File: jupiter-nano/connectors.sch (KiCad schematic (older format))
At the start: 21 parts, among them J1 USB_B_Micro, J2 USB_B_Micro, J3 Conn_ARM_JTAG_SWD_10, J4 USB_B_Micro, J5 Micro_SD_Card_Det_Hirose_DM3AT, J6 Conn_01x02

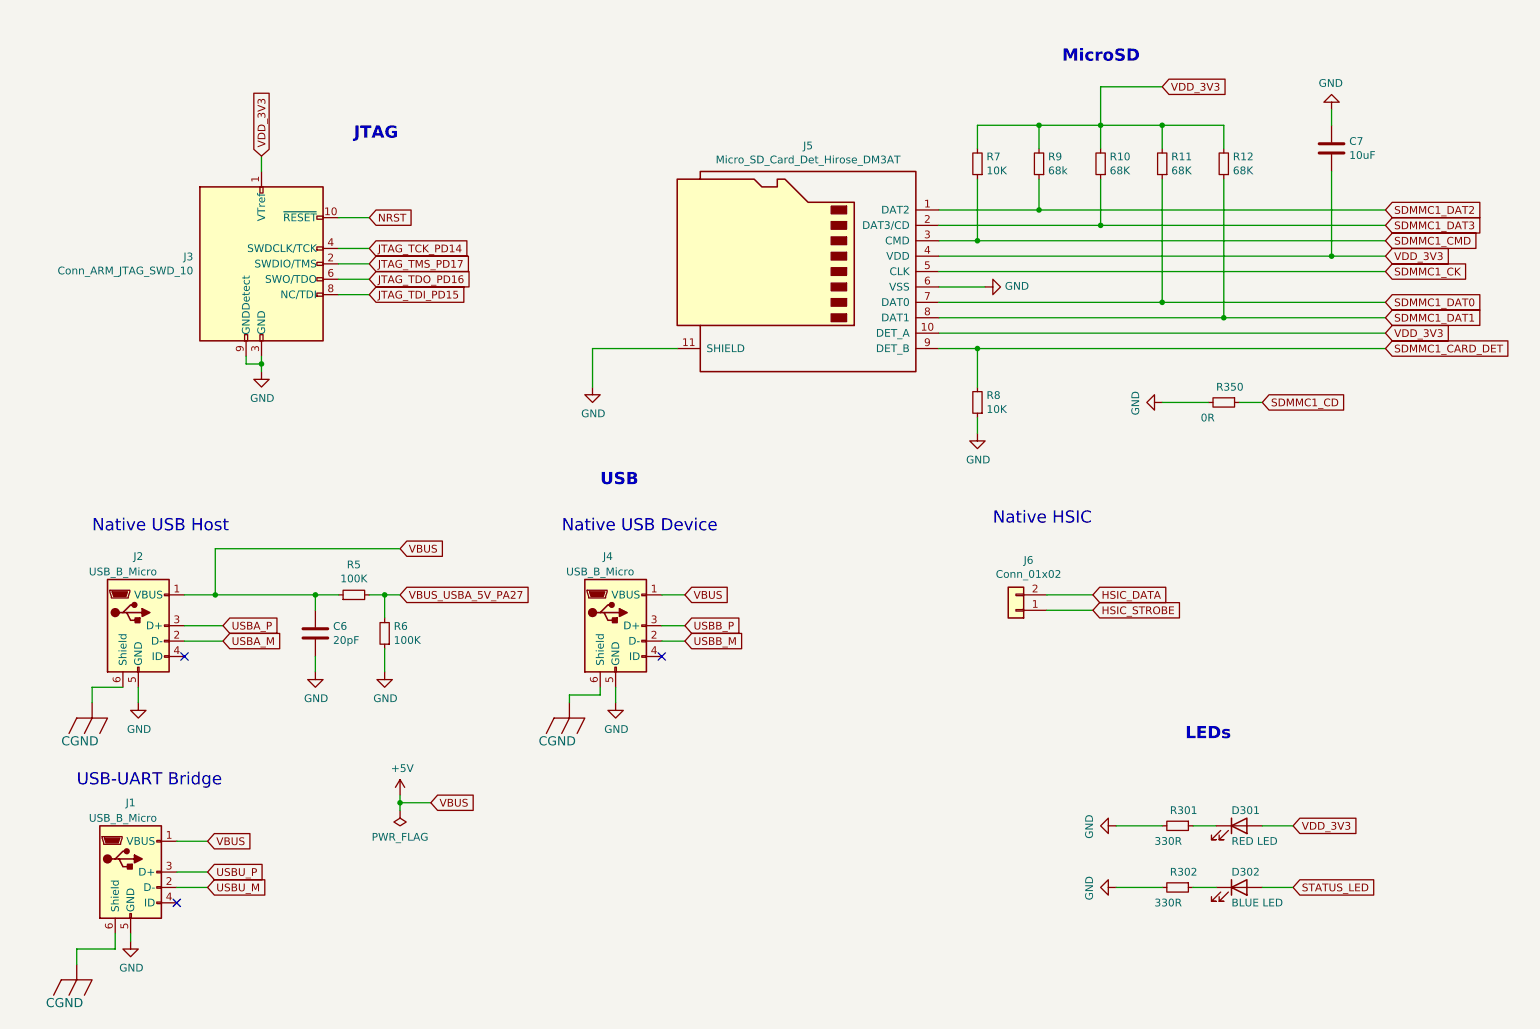
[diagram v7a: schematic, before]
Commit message: added at24csw080 I2C EEPROM UUID chip
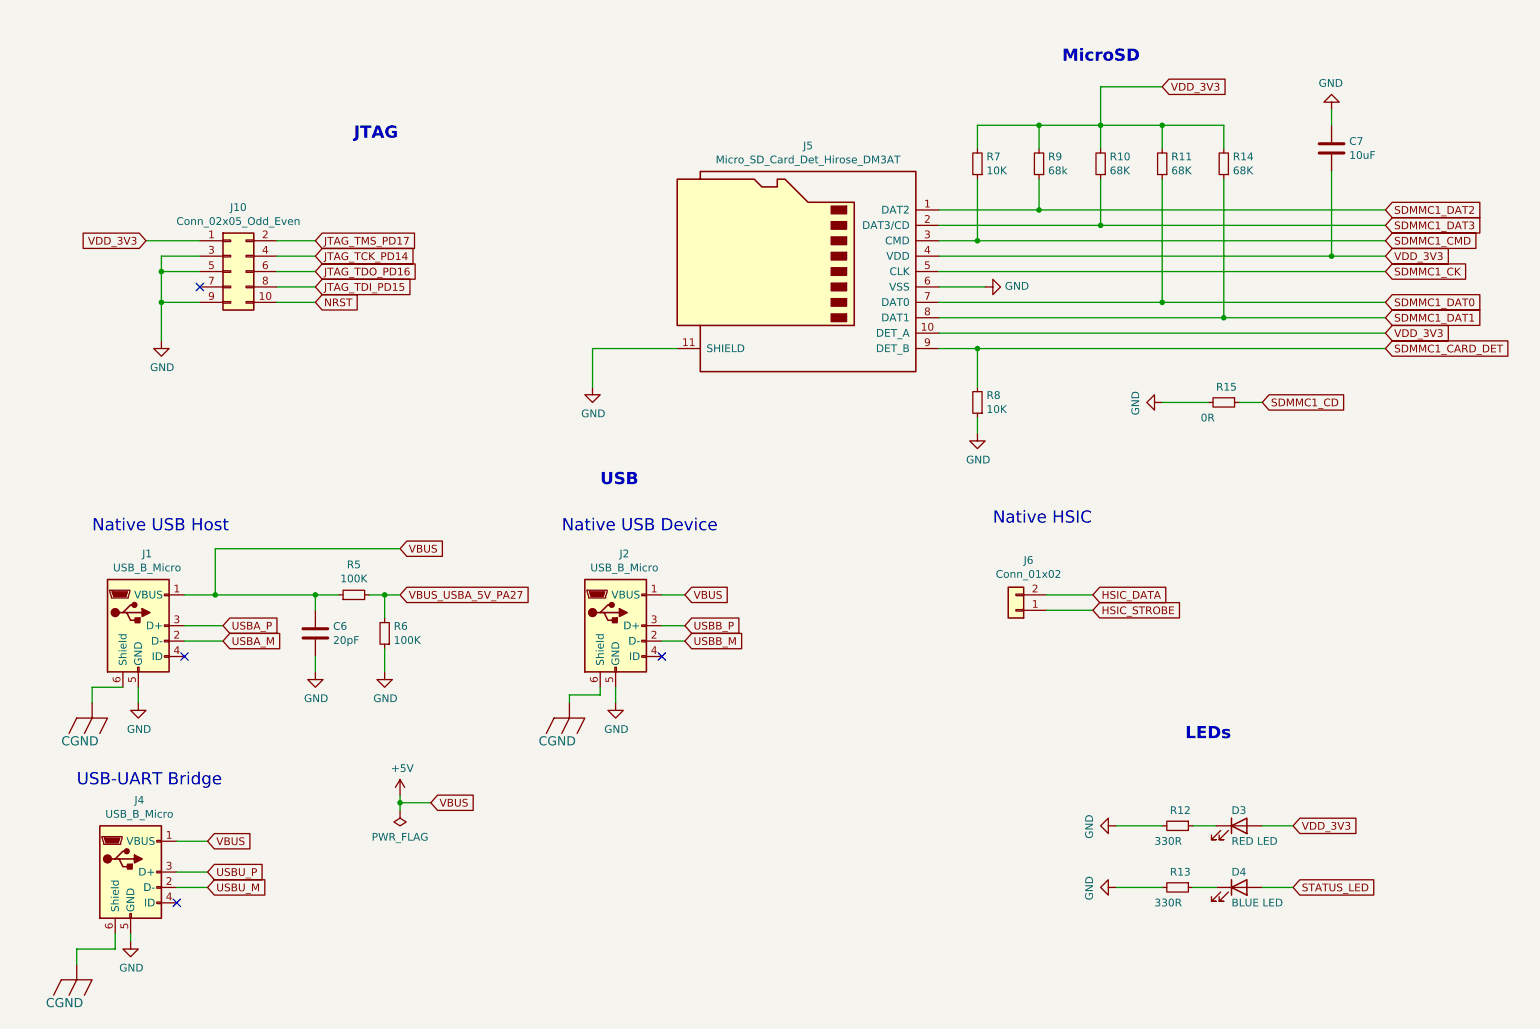
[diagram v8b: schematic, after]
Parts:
- removed J1, J2, J4: USB_B_Micro, symbol Connector:USB_B_Micro
- removed J3: Conn_ARM_JTAG_SWD_10, symbol Connector:Conn_ARM_JTAG_SWD_10
- added J1, J2, J4: USB_B_Micro, symbol starcat:USB_B_Micro
- added J10: Conn_02x05_Odd_Even, symbol Connector_Generic:Conn_02x05_Odd_Even
- renumbered D301 to D3, D302 to D4, R301 to R12, R302 to R13, R12 to R14, R350 to R15
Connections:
- net +5V: now also J1.1 (VBUS), J2.1 (VBUS), J4.1 (VBUS)
- net CGND: now also J1.6 (Shield), J2.6 (Shield), J4.6 (Shield)
- net GND: now also J1.5 (GND), J10.3 (Pin_3), J10.5 (Pin_5), J10.9 (Pin_9), J2.5 (GND), J4.5 (GND)
- net JTAG_TCK_PD14: now also J10.4 (Pin_4)
- net JTAG_TDI_PD15: now also J10.8 (Pin_8)
- net JTAG_TDO_PD16: now also J10.6 (Pin_6)
- net JTAG_TMS_PD17: now also J10.2 (Pin_2)
- net NRST: now also J10.10 (Pin_10)
- net USBA_M: now also J1.2 (D-)
- net USBA_P: now also J1.3 (D+)
- net USBB_M: now also J2.2 (D-)
- net USBB_P: now also J2.3 (D+)
- net USBU_M: now also J4.2 (D-)
- net USBU_P: now also J4.3 (D+)
- net VDD_3V3: now also J10.1 (Pin_1)
- no-connect marks 3 -> 4
